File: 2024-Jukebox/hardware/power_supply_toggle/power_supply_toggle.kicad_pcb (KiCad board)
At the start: 2 copper layers, 20 x 20 mm, 6 parts, among them J1 Conn_01x02, J2 Conn_01x02, J3 Conn_01x02, U1 74HC74

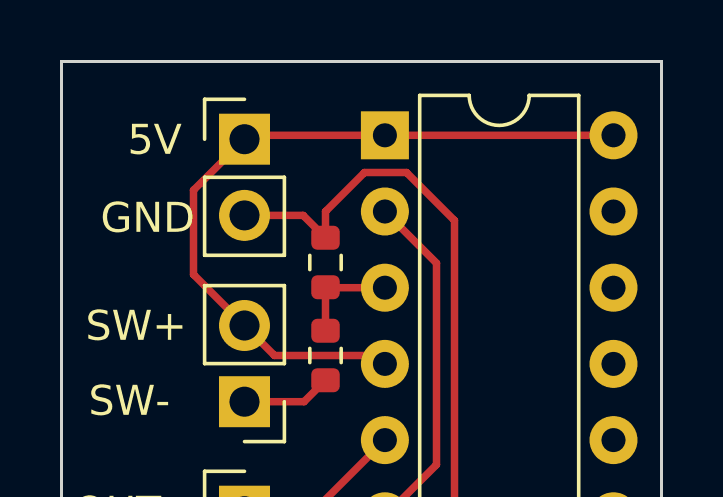
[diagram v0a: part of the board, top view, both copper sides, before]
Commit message: Added decoupling cap to power supply toggle board
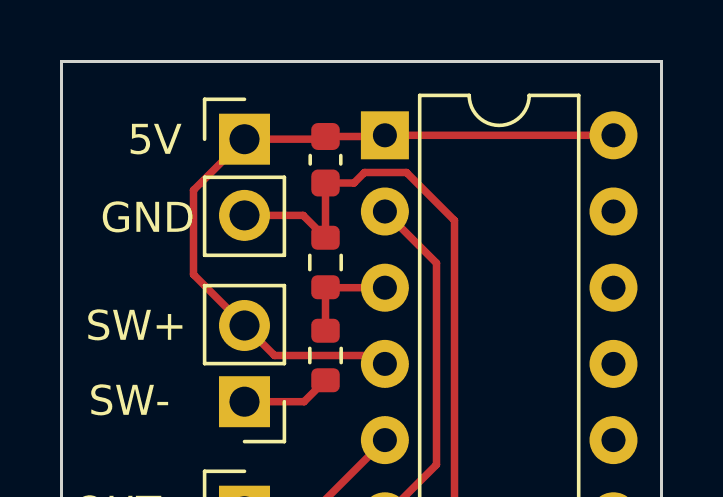
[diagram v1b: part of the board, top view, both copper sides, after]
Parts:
- added C1: 100n, Capacitor_SMD:C_0603_1608Metric, F.Cu at (110.4, 59.8)
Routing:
- net GND: track 27.5 -> 28.1 mm
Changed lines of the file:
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@@
   (net 11 "unconnected-(U1B-D-Pad12)")
   (net 12 "unconnected-(U1B-~{R}-Pad13)")
+  (footprint "Capacitor_SMD:C_0603_1608Metric" (layer "F.Cu")
+    (at 110.4 59.775 -90)
+    (descr "Capacitor SMD 0603 (1608 Metric), square (rectangular) end terminal, IPC_7351 nominal, (Body size source: IPC-SM-782 page 76, https://www.pcb-3d.com/wordpress/wp-content/uploads/ipc-sm-782a_amendment_1_and_2.pdf), generated with kicad-footprint-generator")
+    (tags "capacitor")
+    (property "Sheetfile" "power_supply_toggle.kicad_sch")
+    (property "Sheetname" "")
+    (property "ki_description" "Unpolarized capacitor")
+    (property "ki_keywords" "cap capacitor")
+    (attr smd)
+    (fp_text reference "C1" (at 0 -1.43 90) (layer "F.SilkS") hide
+        (effects (font (size 1 1) (thickness 0.15)))
+    )
+    (fp_text value "100n" (at 0 1.43 90) (layer "F.Fab")
+        (effects (font (size 1 1) (thickness 0.15)))
+    )
+    (fp_text user "${REFERENCE}" (at 0 0 90) (layer "F.Fab")
+        (effects (font (size 0.4 0.4) (thickness 0.06)))
+    )
+    (fp_line (start -0.14058 -0.51) (end 0.14058 -0.51)
+      (stroke (width 0.12) (type solid)) (layer "F.SilkS"))
+    (fp_line (start -0.14058 0.51) (end 0.14058 0.51)
+      (stroke (width 0.12) (type solid)) (layer "F.SilkS"))
+    (fp_line (start -1.48 -0.73) (end 1.48 -0.73)
+      (stroke (width 0.05) (type solid)) (layer "F.CrtYd"))
+    (fp_line (start -1.48 0.73) (end -1.48 -0.73)
+      (stroke (width 0.05) (type solid)) (layer "F.CrtYd"))
+    (fp_line (start 1.48 -0.73) (end 1.48 0.73)
+      (stroke (width 0.05) (type solid)) (layer "F.CrtYd"))
+    (fp_line (start 1.48 0.73) (end -1.48 0.73)
+      (stroke (width 0.05) (type solid)) (layer "F.CrtYd"))
+    (fp_line (start -0.8 -0.4) (end 0.8 -0.4)
+      (stroke (width 0.1) (type solid)) (layer "F.Fab"))
+    (fp_line (start -0.8 0.4) (end -0.8 -0.4)
+      (stroke (width 0.1) (type solid)) (layer "F.Fab"))
+    (fp_line (start 0.8 -0.4) (end 0.8 0.4)
+      (stroke (width 0.1) (type solid)) (layer "F.Fab"))
+    (fp_line (start 0.8 0.4) (end -0.8 0.4)
+      (stroke (width 0.1) (type solid)) (layer "F.Fab"))
+    (pad "1" smd roundrect (at -0.775 0 270) (size 0.9 0.95) (layers "F.Cu" "F.Paste" "F.Mask") (roundrect_rratio 0.25)
+      (net 3 "+5V") (pintype "passive"))
+    (pad "2" smd roundrect (at 0.775 0 270) (size 0.9 0.95) (layers "F.Cu" "F.Paste" "F.Mask") (roundrect_rratio 0.25)
+      (net 2 "GND") (pintype "passive"))
+    (model "${KICAD6_3DMODEL_DIR}/Capacitor_SMD.3dshapes/C_0603_1608Metric.wrl"
+      (offset (xyz 0 0 0))
+      (scale (xyz 1 1 1))
+      (rotate (xyz 0 0 0))
+    )
+  )
   (footprint "Connector_PinHeader_2.54mm:PinHeader_1x02_P2.54mm_Vertical" (layer "F.Cu")
     (at 107.7 67.84 180)
@@
   (segment (start 114.7 71.88) (end 114.7 61.8) (width 0.25) (layer "F.Cu") (net 2))
   (segment (start 113.1 60.2) (end 111.7 60.2) (width 0.25) (layer "F.Cu") (net 2))
-  (segment (start 110.4 61.5) (end 110.4 62.375) (width 0.25) (layer "F.Cu") (net 2))
+  (segment (start 110.4 60.55) (end 110.4 62.375) (width 0.25) (layer "F.Cu") (net 2))
   (segment (start 112.38 74.2) (end 114.7 71.88) (width 0.25) (layer "F.Cu") (net 2))
-  (segment (start 111.7 60.2) (end 110.4 61.5) (width 0.25) (layer "F.Cu") (net 2))
+  (segment (start 111.7 60.2) (end 111.35 60.55) (width 0.25) (layer "F.Cu") (net 2))
   (segment (start 112.21 74.03) (end 112.38 74.2) (width 0.25) (layer "F.Cu") (net 2))
+  (segment (start 111.35 60.55) (end 110.4 60.55) (width 0.25) (layer "F.Cu") (net 2))
   (segment (start 109.655 61.63) (end 110.4 62.375) (width 0.25) (layer "F.Cu") (net 2))
+  (segment (start 110.31 59.09) (end 110.4 59) (width 0.25) (layer "F.Cu") (net 3))
   (segment (start 106 63.6) (end 106 60.79) (width 0.25) (layer "F.Cu") (net 3))
   (segment (start 120 58.96) (end 112.38 58.96) (width 0.25) (layer "F.Cu") (net 3))
   (segment (start 107.7 65.3) (end 108.7 66.3) (width 0.25) (layer "F.Cu") (net 3))
   (segment (start 112.1 66.3) (end 112.38 66.58) (width 0.25) (layer "F.Cu") (net 3))
-  (segment (start 112.38 58.96) (end 107.83 58.96) (width 0.25) (layer "F.Cu") (net 3))
   (segment (start 107.83 58.96) (end 107.7 59.09) (width 0.25) (layer "F.Cu") (net 3))
   (segment (start 108.7 66.3) (end 112.1 66.3) (width 0.25) (layer "F.Cu") (net 3))
   (segment (start 107.7 65.3) (end 106 63.6) (width 0.25) (layer "F.Cu") (net 3))
+  (segment (start 107.7 59.09) (end 110.31 59.09) (width 0.25) (layer "F.Cu") (net 3))
+  (segment (start 110.4 59) (end 112.34 59) (width 0.25) (layer "F.Cu") (net 3))
+  (segment (start 112.34 59) (end 112.38 58.96) (width 0.25) (layer "F.Cu") (net 3))
   (segment (start 106 60.79) (end 107.7 59.09) (width 0.25) (layer "F.Cu") (net 3))
   (segment (start 107.7 67.84) (end 109.685 67.84) (width 0.25) (layer "F.Cu") (net 4))

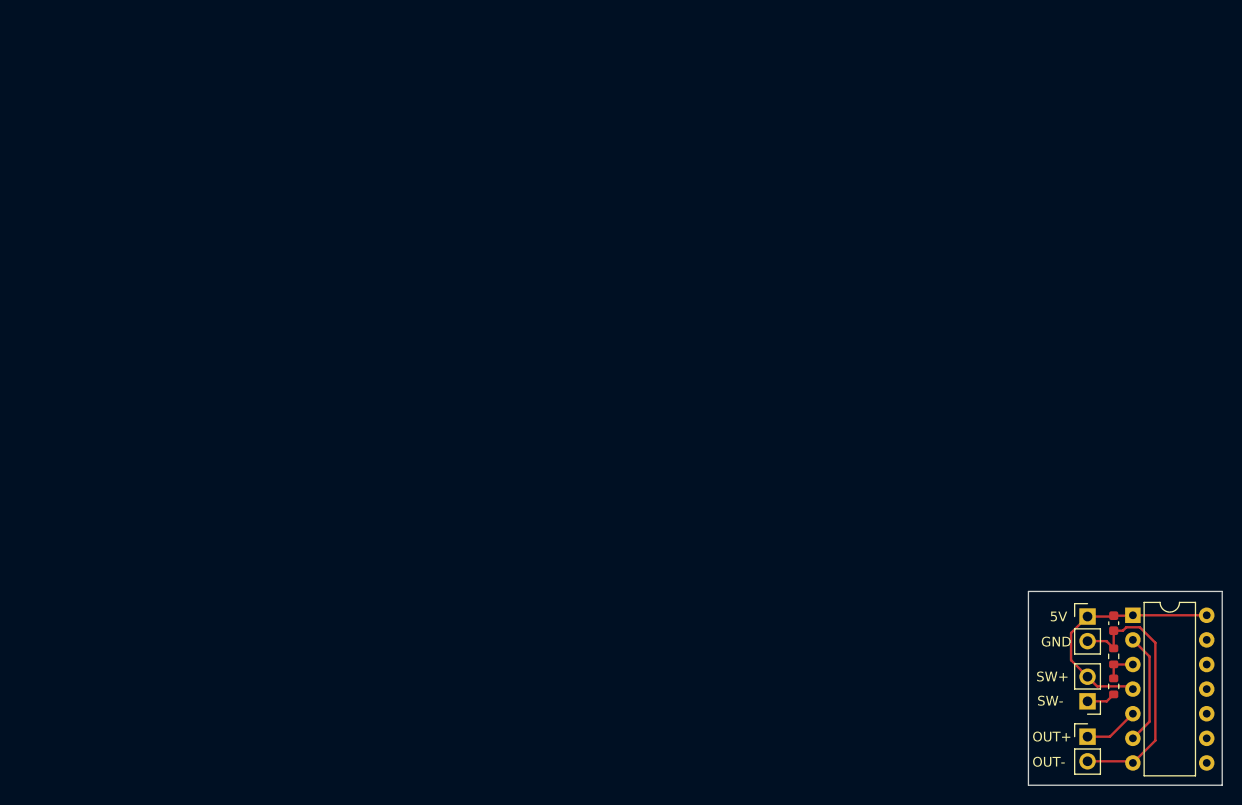
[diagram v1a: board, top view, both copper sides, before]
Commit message: Updated power supply toggle pcb
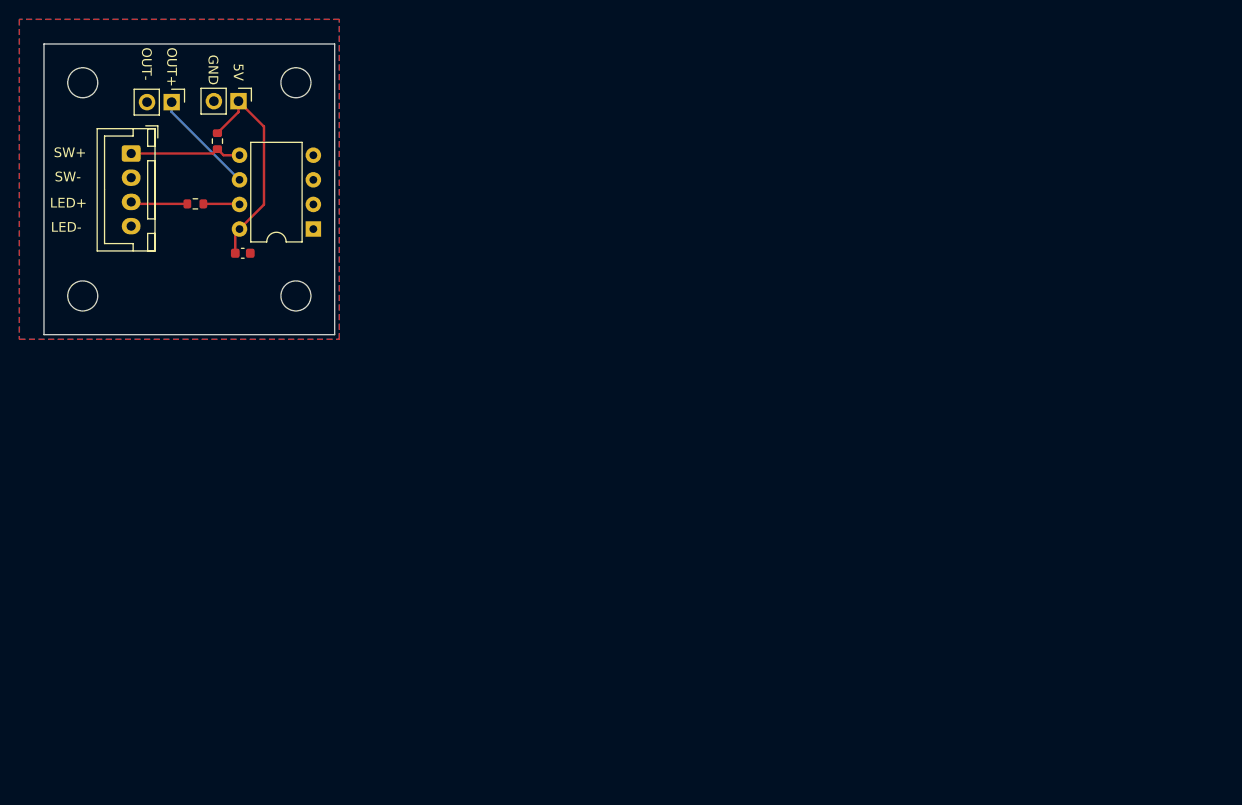
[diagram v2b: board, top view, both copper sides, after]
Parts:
- removed J3: Conn_01x02, Connector_PinHeader_2.54mm:PinHeader_1x02_P2.54mm_Vertical
- added J4: Conn_01x04, Connector_JST:JST_XH_B4B-XH-A_1x04_P2.50mm_Vertical, F.Cu at (9.00, 11.3)
- R1: value 10k -> 1k
- U1: value 74HC74 -> ATtiny85-20P; footprint Package_DIP:DIP-14_W7.62mm -> Package_DIP:DIP-8_W7.62mm
- moved J1 115.0 mm to (13.2, 6.00), turned to -90 degrees
- moved R2 108.3 mm to (17.9, 10.0), turned to -90 degrees
- moved R1 105.7 mm to (15.6, 16.5), turned to 180 degrees
- moved J2 102.5 mm to (20.1, 5.90), turned to -90 degrees
- moved C1 97.7 mm to (20.5, 21.6), turned to 0 degrees
- moved U1 93.5 mm to (27.8, 19.1), turned to 180 degrees
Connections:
- R1 pad 1: Net-(U1A-C) -> Net-(U1-PB2)
- R1 pad 2: GND -> Net-(J4-Pin_3)
- R2 pad 1: Net-(J3-Pin_1) -> +5V
- R2 pad 2: Net-(U1A-C) -> Net-(J4-Pin_1)
- U1 pad 1: +5V -> unconnected-(U1-~{RESET}/PB5-Pad1)
- U1 pad 2: Net-(U1A-D) -> unconnected-(U1-XTAL1/PB3-Pad2)
- U1 pad 3: Net-(U1A-C) -> unconnected-(U1-XTAL2/PB4-Pad3)
- U1 pad 4: +5V -> GND
- U1 pad 5: Net-(J1-Pin_1) -> Net-(J4-Pin_1)
- U1 pad 6: Net-(U1A-D) -> Net-(J1-Pin_1)
- U1 pad 7: GND -> Net-(U1-PB2)
- U1 pad 8: unconnected-(U1B-~{Q}-Pad8) -> +5V
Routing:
- net GND: track 28.1 -> 0.00 mm
- net Net-(J4-Pin_1): track 0.00 -> 11.6 mm
- net Net-(U1A-D): track 11.6 -> 0.00 mm
- net Net-(J4-Pin_3): track 0.00 -> 5.88 mm
- net Net-(J1-Pin_1): track 5.66 -> 10.9 mm
- net Net-(U1-PB2): track 0.00 -> 3.75 mm
- net Net-(U1A-C): track 3.44 -> 0.00 mm
- net +5V: track 25.4 -> 22.2 mm
- net Net-(J3-Pin_1): track 3.00 -> 0.00 mm
- added copper zone on B.Cu, net GND
- added copper zone on F.Cu, net GND
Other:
- board size 20 x 20 mm -> 30 x 30 mm
- board text added: "LED+"
- board text added: "LED-"
